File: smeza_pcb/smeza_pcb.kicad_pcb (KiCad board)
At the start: 2 copper layers, 76.2 x 76.2 mm, 54 parts, among them J1 SS-90000-002, J2 SS-90000-002, J3 Conn_01x03, J4 Conn_01x04, J5 Conn_01x03, J6 Conn_01x03, J7 Conn_01x03, J8 Conn_01x03, J9 Conn_02x03_Odd_Even, SW1 SW_DIP_x04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

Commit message: Corrected Footprints in Schematic. Reorganized passives supporting the buck converter. Rerouted 50V passthough, D+/- passthrough.
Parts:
- B1: value SOIC127P600X170-9N -> MP4541GN-Z
- SW1, SW2: footprint Button_Switch_THT:SW_DIP_SPSTx04_Slide_9.78x12.34mm_W7.62mm_P2.54mm -> Button_Switch_SMD:SW_DIP_SPSTx04_Slide_6.7x11.72mm_W8.61mm_P2.54mm_LowProfile
- SW3: footprint Button_Switch_THT:SW_DIP_SPSTx01_Slide_9.78x4.72mm_W7.62mm_P2.54mm -> Button_Switch_SMD:SW_DIP_SPSTx01_Slide_6.7x4.1mm_W8.61mm_P2.54mm_LowProfile
- T1: value (none) -> ADM4852ARZ
- moved R18 25.5 mm to (145.3, 123.9), turned to -90 degrees
- moved R1 23.9 mm to (142.7, 124.0), turned to 90 degrees
- moved C1 19.9 mm to (141.2, 119.9), turned to 180 degrees
- moved R8 8.69 mm to (132.4, 121.9), turned to 90 degrees
- moved C2B1 7.52 mm to (144.7, 109.7), turned to 180 degrees
- moved SW2 5.77 mm to (123.2, 78.0)
- moved R2 4.24 mm to (140.2, 124.0)
- moved L1 3.16 mm to (140.8, 104.9), turned to 180 degrees
- moved B1 3.09 mm to (136.7, 114.8)
- moved R9 2.72 mm to (132.4, 117.2), turned to -90 degrees
- moved C3 2.64 mm to (139.7, 109.7)
- moved C6 2.59 mm to (135.3, 121.2)
- moved R7 2.59 mm to (137.8, 121.2)
- moved C2 2.54 mm to (134.7, 109.7)
- moved C2A1 1.94 mm to (147.9, 104.1), turned to 0 degrees
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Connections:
- net Net-(B1-VCC) renamed /BuckConverterVCC
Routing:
- net Net-(B1-FB): track 38.8 -> 8.19 mm
- net /Buck+5V: track 22.6 -> 43.2 mm
- net /+50V: track 68.9 -> 85.0 mm, vias 3 -> 1
- net /D-: track 68.7 -> 81.5 mm, vias 0 -> 1
- net /D+: track 75.1 -> 84.9 mm, vias 0 -> 1
- net GND: track 25.9 -> 28.5 mm, vias 99 -> 17
- net Net-(B1-EN): track 5.74 -> 4.58 mm
- net Net-(R1-Pad1): track 3.17 -> 2.57 mm
- added copper zone on F.Cu, net /Buck+5V
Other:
- board text added: "SMEZA V0.2"
- board text removed: "SMEZA V0.1"

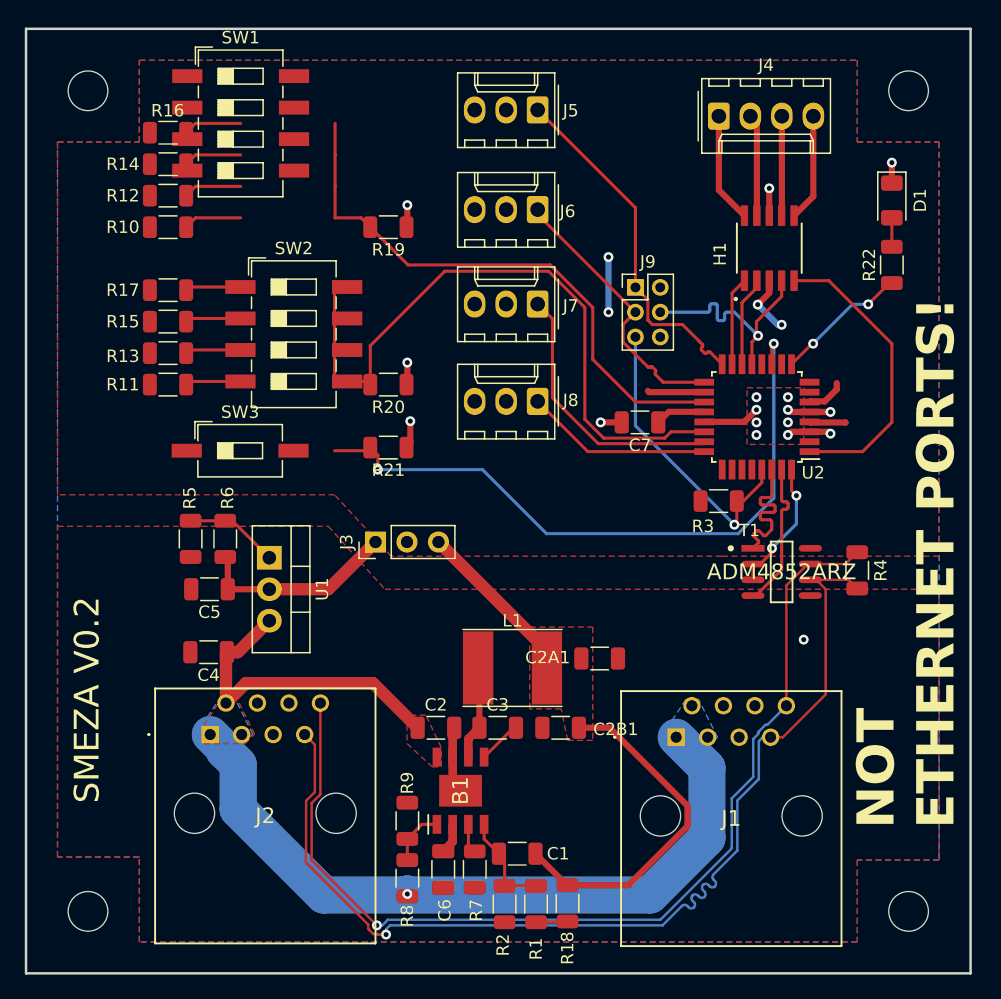
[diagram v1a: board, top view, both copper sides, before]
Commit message: Reorganized all components and rerouted. Added capacitors to H-Bridge. Added Capacitors to dip switches. Updated DIP switch footprint. Fixed DRC and ERC errors.
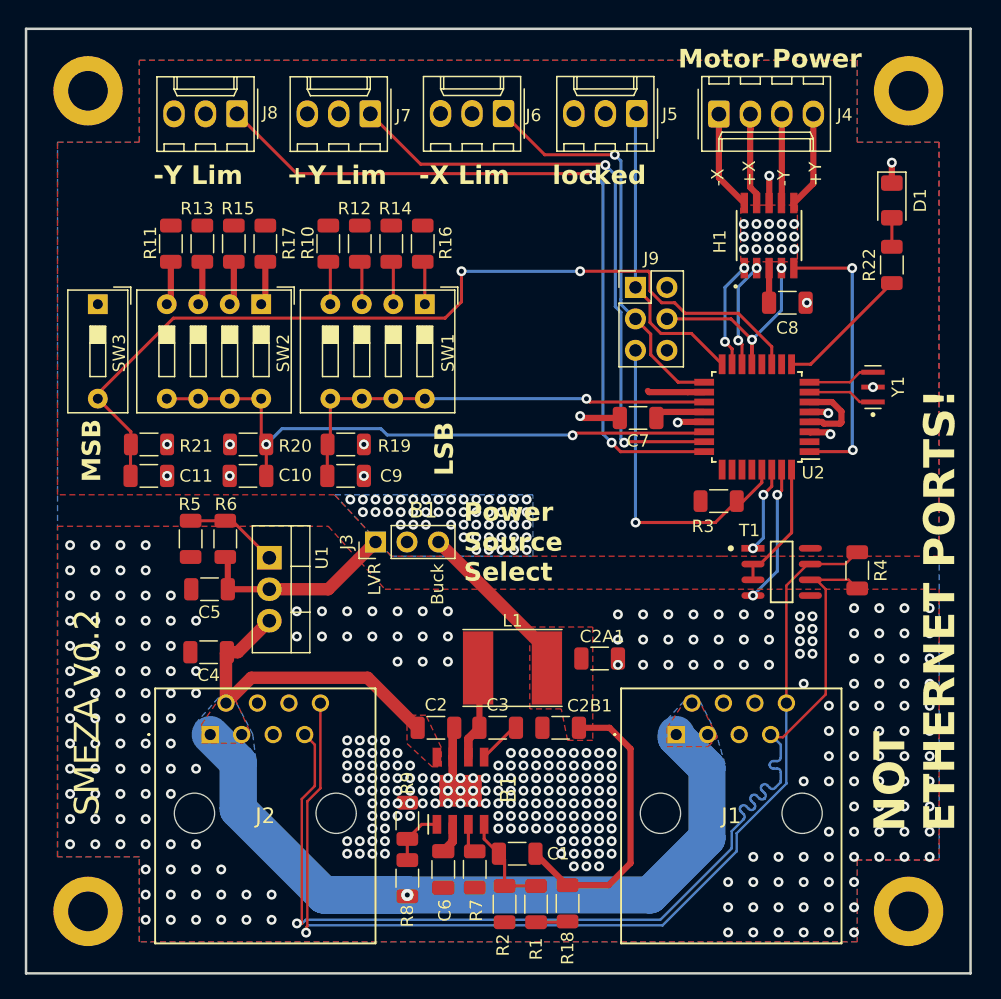
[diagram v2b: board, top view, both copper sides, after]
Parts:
- added C10: 1nF, Capacitor_SMD:C_1206_3216Metric, F.Cu at (119.5, 89.4)
- added C11: 1nF, Capacitor_SMD:C_1206_3216Metric, F.Cu at (111.5, 89.4)
- added C8: 10uF, Capacitor_SMD:C_1206_3216Metric, F.Cu at (163.0, 75.4)
- added C9: 1nF, Capacitor_SMD:C_1206_3216Metric, F.Cu at (127.4, 89.4)
- added Y1: CSTNE16M0V530000R0, Footprints:OSC_CSTNE16M0V530000R0, F.Cu at (169.9, 82.2)
- J9: footprint Connector_PinHeader_2.00mm:PinHeader_2x03_P2.00mm_Vertical -> Connector_PinHeader_2.54mm:PinHeader_2x03_P2.54mm_Vertical
- R4: value DNP -> 120
- REF** (x4): value MountingHole_3.2mm_M3_DIN965 -> MountingHole_3.2mm_M3_DIN965_Pad; footprint MountingHole:MountingHole_3.2mm_M3_DIN965 -> MountingHole:MountingHole_3.2mm_M3_DIN965_Pad
- SW1, SW2: footprint Button_Switch_SMD:SW_DIP_SPSTx04_Slide_6.7x11.72mm_W8.61mm_P2.54mm_LowProfile -> Button_Switch_THT:SW_DIP_SPSTx04_Slide_9.78x12.34mm_W7.62mm_P2.54mm
- SW3: footprint Button_Switch_SMD:SW_DIP_SPSTx01_Slide_6.7x4.1mm_W8.61mm_P2.54mm_LowProfile -> Button_Switch_THT:SW_DIP_SPSTx01_Slide_9.78x4.72mm_W7.62mm_P2.54mm
- moved J8 33.6 mm to (118.6, 60.2)
- moved R16 22.4 mm to (133.6, 70.7), turned to -90 degrees
- moved SW1 20.8 mm to (133.8, 75.6), turned to -90 degrees
- moved J7 20.4 mm to (129.4, 60.2)
- moved R21 19.3 mm to (111.5, 86.9)
- moved R14 19.1 mm to (131.1, 70.7), turned to -90 degrees
- moved R19 17.9 mm to (127.4, 86.9)
- moved SW3 16.5 mm to (107.4, 75.6), turned to -90 degrees
- moved R12 15.9 mm to (128.5, 70.7), turned to -90 degrees
- moved R10 13.0 mm to (126.0, 70.7), turned to -90 degrees
- moved R20 12.3 mm to (119.5, 86.9), turned to 0 degrees
- moved R11 11.4 mm to (113.3, 70.7), turned to -90 degrees
- moved R13 9.25 mm to (115.8, 70.7), turned to -90 degrees
- moved R17 8.70 mm to (120.9, 70.7), turned to -90 degrees
- moved R15 8.23 mm to (118.4, 70.7), turned to -90 degrees
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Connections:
- U2 pad 7: unconnected-(U2-XTAL1/PB6-Pad7) -> Net-(U2-XTAL1/PB6)
- U2 pad 8: unconnected-(U2-XTAL2/PB7-Pad8) -> Net-(U2-XTAL2/PB7)
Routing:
- net /M2 -Limit: track 15.1 -> 60.8 mm, vias 0 -> 2
- net /M2 +Limit: track 21.9 -> 50.2 mm, vias 0 -> 2
- net /DIP9: track 54.5 -> 72.4 mm
- net /M1 -Limit (SCK): track 22.5 -> 32.9 mm, vias 0 -> 1
- net /DIPS14: track 46.0 -> 36.6 mm, vias 0 -> 1
- net GND: track 28.5 -> 19.6 mm, vias 17 -> 375
- net /+50V: track 85.0 -> 92.3 mm
- net /+5V: track 20.0 -> 13.8 mm, vias 4 -> 50
- net Net-(U2-XTAL2/PB7): track 0.00 -> 5.45 mm
- net Net-(U2-XTAL1/PB6): track 0.00 -> 5.45 mm
- net /D-: track 81.5 -> 86.8 mm
- net /D+: track 84.9 -> 90.1 mm
- net /Rx: track 11.9 -> 6.98 mm, vias 0 -> 2
- net /Buck+5V: track 43.2 -> 38.4 mm
- net /DIPS58: track 54.2 -> 50.2 mm, vias 0 -> 2
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- added copper zone on B.Cu, net /+5V
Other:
- board text added: "+X"
- board text added: "+Y"
- board text added: "+Y Lim"
- board text added: "-X"
- board text added: "-X Lim"
- board text added: "-Y"
- board text added: "-Y Lim"
- board text added: "B1"
- board text added: "Buck"
- board text added: "LSB"
- board text added: "LVR"
- board text added: "MSB"
- board text added: "Motor Power"
- board text added: "Power Source Select"
- board text added: "locked"

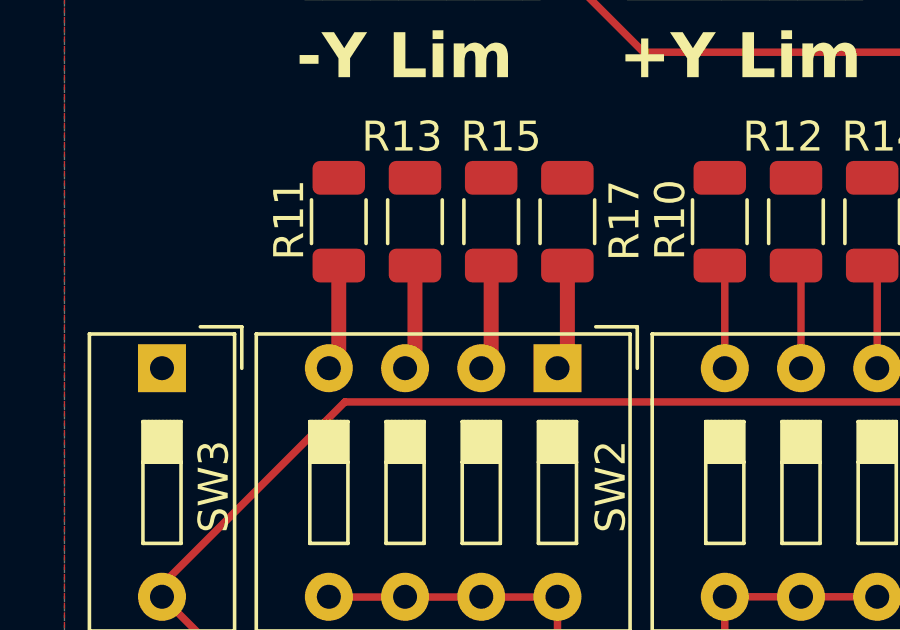
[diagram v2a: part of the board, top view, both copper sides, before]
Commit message: Resized traces for SW2.
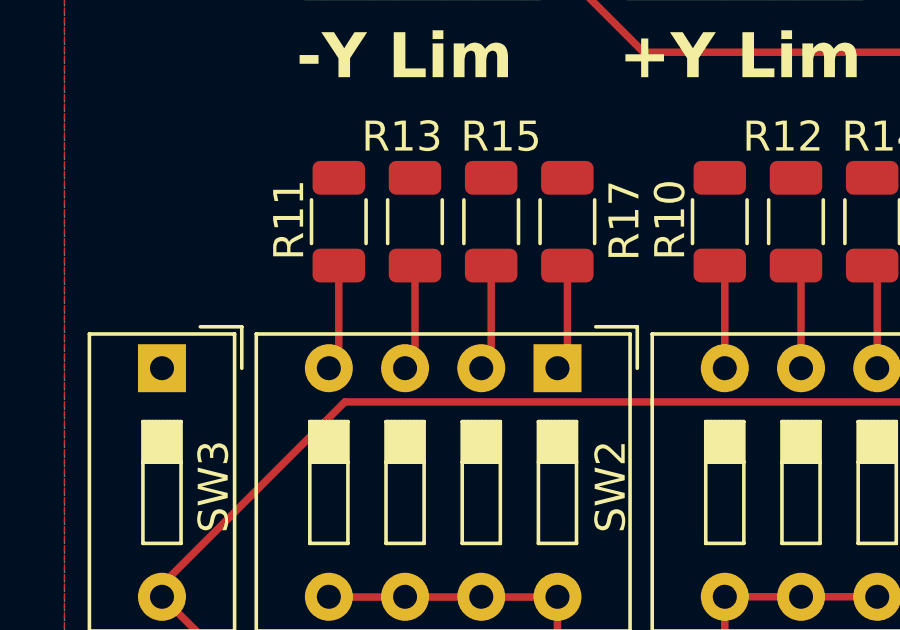
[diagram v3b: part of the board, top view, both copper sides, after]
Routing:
- net Net-(R15-Pad2): track 2.85 -> 3.56 mm
- net Net-(R13-Pad2): track 2.85 -> 3.56 mm
- net Net-(R11-Pad2): track 2.85 -> 3.56 mm
- net Net-(R17-Pad2): track 2.85 -> 3.56 mm
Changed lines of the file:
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@@
   (segment (start 126.1518 75.5567) (end 126.1518 72.3038) (width 0.25) (layer "F.Cu") (net 14))
   (segment (start 126.1518 72.3038) (end 125.984 72.136) (width 0.25) (layer "F.Cu") (net 14))
-  (segment (start 113.284 72.136) (end 113.284 74.9909) (width 0.5) (layer "F.Cu") (net 15))
+  (segment (start 113.284 75.2265) (end 112.9538 75.5567) (width 0.25) (layer "F.Cu") (net 15))
+  (segment (start 113.284 72.136) (end 113.284 75.2265) (width 0.25) (layer "F.Cu") (net 15))
   (segment (start 128.6918 75.5567) (end 128.6918 72.3038) (width 0.25) (layer "F.Cu") (net 16))
   (segment (start 128.6918 72.3038) (end 128.524 72.136) (width 0.25) (layer "F.Cu") (net 16))
-  (segment (start 115.824 72.136) (end 115.824 74.9909) (width 0.5) (layer "F.Cu") (net 17))
+  (segment (start 115.824 72.136) (end 115.824 75.2265) (width 0.25) (layer "F.Cu") (net 17))
+  (segment (start 115.824 75.2265) (end 115.4938 75.5567) (width 0.25) (layer "F.Cu") (net 17))
   (segment (start 131.2318 72.3038) (end 131.064 72.136) (width 0.25) (layer "F.Cu") (net 18))
   (segment (start 131.2318 75.5567) (end 131.2318 72.3038) (width 0.25) (layer "F.Cu") (net 18))
-  (segment (start 118.364 72.136) (end 118.364 74.9909) (width 0.5) (layer "F.Cu") (net 19))
+  (segment (start 118.364 75.2265) (end 118.0338 75.5567) (width 0.25) (layer "F.Cu") (net 19))
+  (segment (start 118.364 72.136) (end 118.364 75.2265) (width 0.25) (layer "F.Cu") (net 19))
   (segment (start 133.7718 72.3038) (end 133.604 72.136) (width 0.25) (layer "F.Cu") (net 20))
   (segment (start 133.7718 75.5567) (end 133.7718 72.3038) (width 0.25) (layer "F.Cu") (net 20))
-  (segment (start 120.904 72.136) (end 120.904 74.9909) (width 0.5) (layer "F.Cu") (net 21))
+  (segment (start 120.904 72.136) (end 120.904 75.2265) (width 0.25) (layer "F.Cu") (net 21))
+  (segment (start 120.904 75.2265) (end 120.5738 75.5567) (width 0.25) (layer "F.Cu") (net 21))
   (segment (start 142.748 125.4145) (end 145.2265 125.4145) (width 0.25) (layer "F.Cu") (net 22))
   (segment (start 145.2265 125.4145) (end 145.288 125.353) (width 0.25) (layer "F.Cu") (net 22))
